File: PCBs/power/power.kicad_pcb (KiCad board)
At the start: 2 copper layers, 30 x 26 mm, 6 parts, among them J1 Barrel_Jack_Switch, J2 Conn_01x06_Male, J3 Conn_01x06_Male, J4 Barrel_Jack_Switch

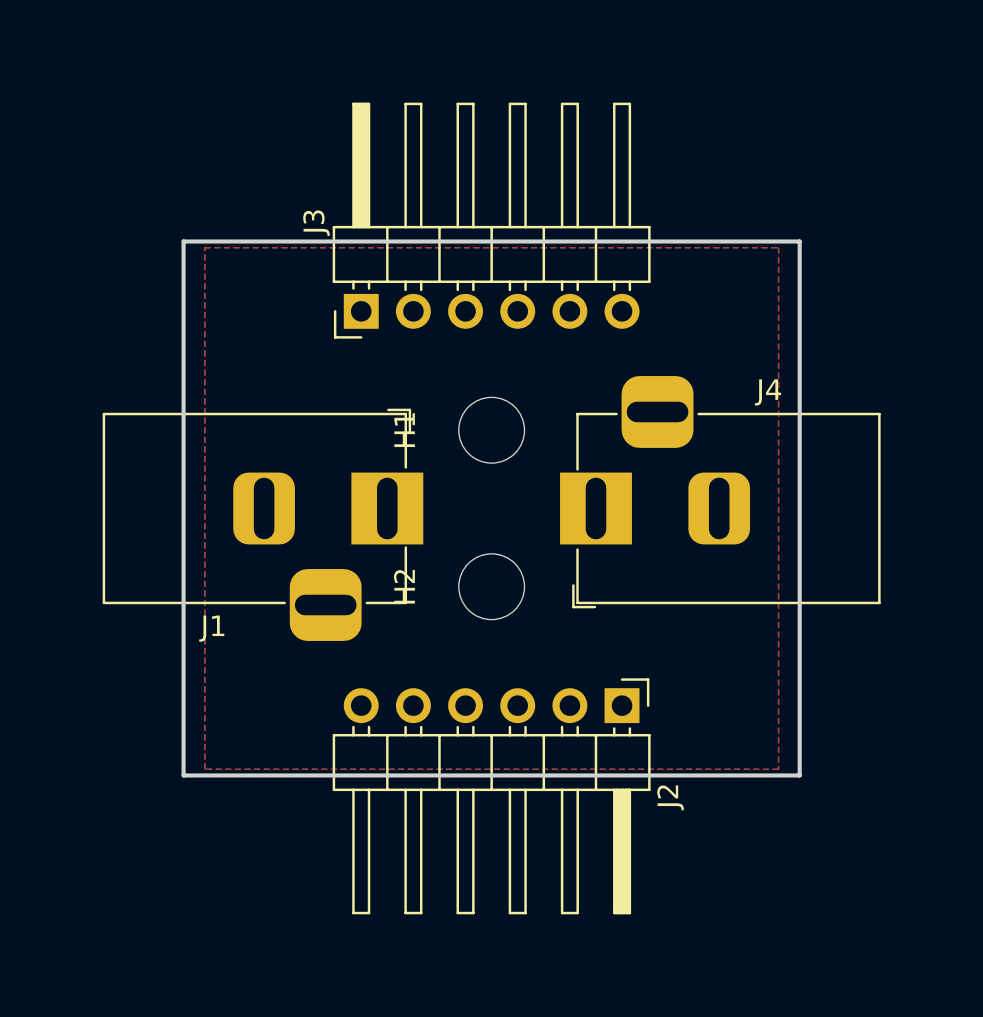
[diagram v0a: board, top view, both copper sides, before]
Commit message: make power pcb bigger
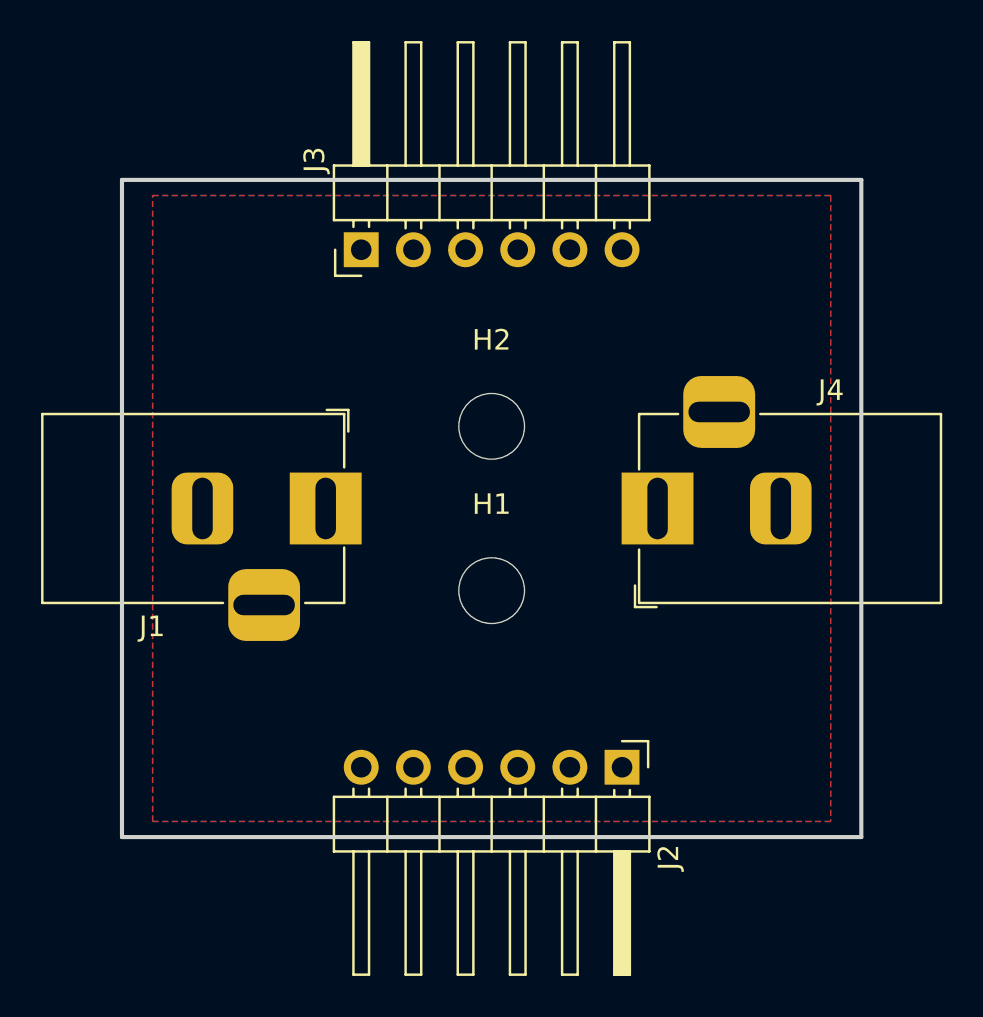
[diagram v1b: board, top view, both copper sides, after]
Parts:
- moved H1 7.81 mm to (141.0, 92.9), turned to 0 degrees
- moved H2 7.81 mm to (141.0, 84.9), turned to 0 degrees
- moved J1 3.00 mm to (132.9, 88.9)
- moved J2 3.00 mm to (147.3, 101.5)
- moved J3 3.00 mm to (134.6, 76.3)
- moved J4 3.00 mm to (149.1, 88.9)
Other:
- board size 30 x 26 mm -> 36 x 32 mm
